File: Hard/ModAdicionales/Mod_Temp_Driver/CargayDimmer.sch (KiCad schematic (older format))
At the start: 18 parts

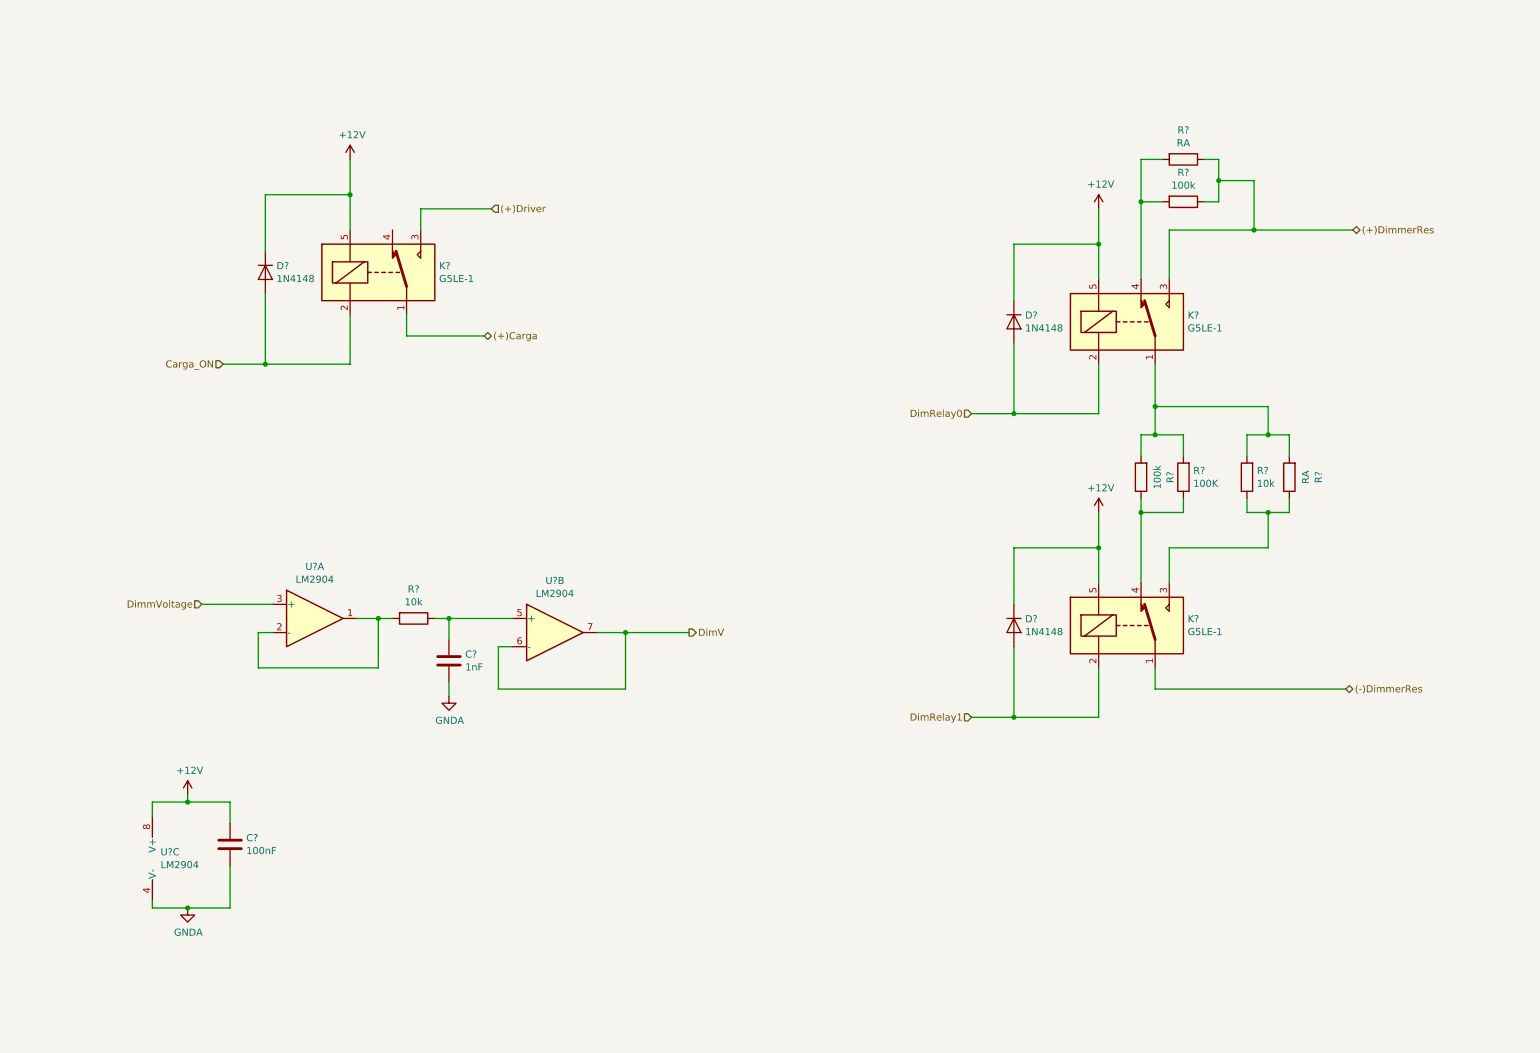
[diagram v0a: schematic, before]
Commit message: Primera correccion en modulos Adicionales y cambio de etapa de salida en modulo principal
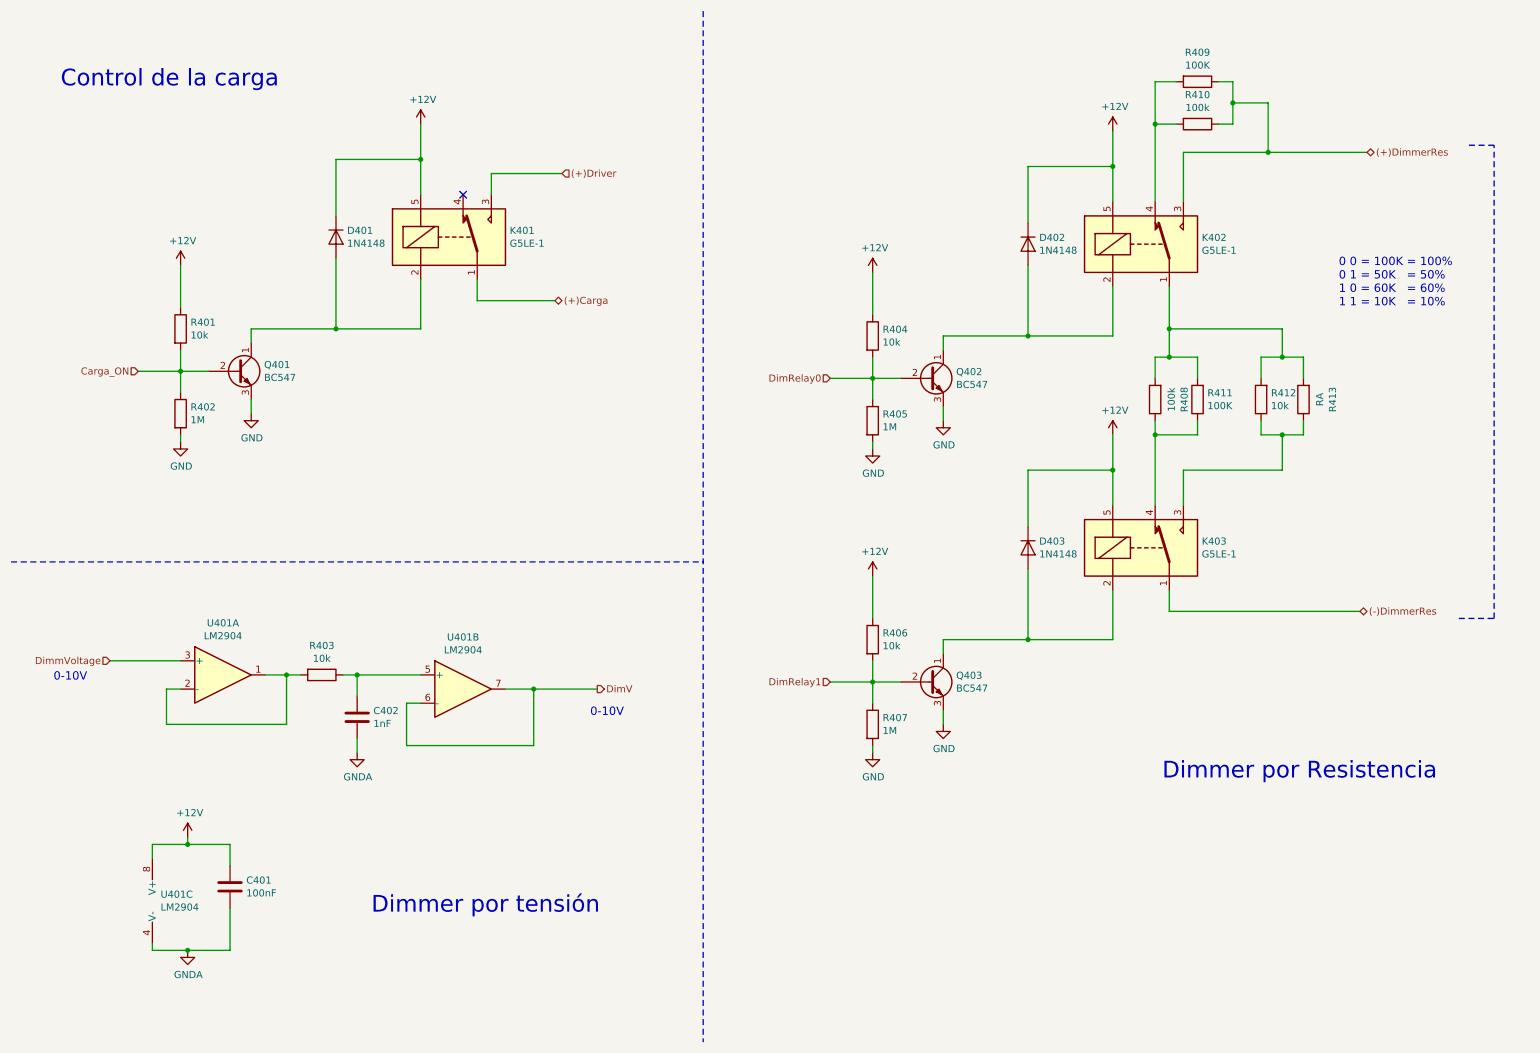
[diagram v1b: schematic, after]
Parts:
- added Q401, Q402, Q403: BC547, Package_TO_SOT_THT:TO-92_Inline, symbol Transistor_BJT:BC547
- added R401, R404, R406: 10k, Resistor_SMD:R_0805_2012Metric_Pad1.15x1.40mm_HandSolder, symbol Device:R
- added R402, R405, R407: 1M, Resistor_SMD:R_0805_2012Metric_Pad1.15x1.40mm_HandSolder, symbol Device:R
- R409: renamed from R?; value RA -> 100K
- gave numbers to parts that had none: 15
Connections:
- net +12V: now also R401.1, R404.1, R406.1
- net Carga_ON: now also Q401.2 (B), R401.2, R402.1; no longer D401.2 (A), K401.2
- net DimRelay0: now also Q402.2 (B), R404.2, R405.1; no longer D402.2 (A), K402.2
- net DimRelay1: now also Q403.2 (B), R406.2, R407.1; no longer D403.2 (A), K403.2
- new net: D402.2 (A), K402.2, Q402.1 (C)
- new net: D403.2 (A), K403.2, Q403.1 (C)
- new net: D401.2 (A), K401.2, Q401.1 (C)
- new net GND: Q401.3 (E), Q402.3 (E), Q403.3 (E), R402.2, R405.2, R407.2
- no-connect marks 0 -> 1
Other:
- note added: "0 0 = 100K = 100%\n0 1 = 50K = 50% \n1 0 = 60K = 60%\n1 1 = 10K = 10%\n"
- note added: "0-10V\n"
- note added: "Control de la carga"
- note added: "Dimmer por Resistencia\n"
- note added: "Dimmer por tensión\n"
- moved on the sheet: C401, C402, D401, D402, D403, K401, K402, K403, R403, R408, R409, R410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

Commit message: Asignacion de footprints Modulos adicionales
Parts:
- removed Q401, Q402, Q403: BC547, Package_TO_SOT_THT:TO-92_Inline, symbol Transistor_BJT:BC547
- added Q401, Q402, Q403: BC857, Package_TO_SOT_SMD:SOT-23, symbol Transistor_BJT:BC857
- R405: value 1M -> 10k
- R406: value 10k -> 1M
- U401: footprint (none) -> Package_SO:SO-8_3.9x4.9mm_P1.27mm
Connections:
- net +12V: now also R402.1, R407.1, Q401.2 (E), Q402.2 (E), Q403.2 (E); no longer D401.1 (K), D402.1 (K), D403.1 (K), K401.5, K402.5, K403.5, R401.1, R404.1
- net Carga_ON: now also R401.1; no longer R401.2, R402.1
- net DimRelay0: now also R404.1; no longer R404.2, R405.1
- net DimRelay1: now also R405.1; no longer R406.2, R407.1
- net GND: now also D401.2 (A), D402.2 (A), D403.2 (A), K401.2, K402.2, K403.2; no longer R402.2, R405.2, R407.2
- new net: Q401.1 (B), R401.2, R402.2
- new net: D401.1 (K), K401.5, Q401.3 (C)
- new net: Q402.1 (B), R404.2, R406.2
- new net: D402.1 (K), K402.5, Q402.3 (C)
- new net: Q403.1 (B), R405.2, R407.2
- new net: D403.1 (K), K403.5, Q403.3 (C)
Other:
- moved on the sheet: D401, K401, R401, R402

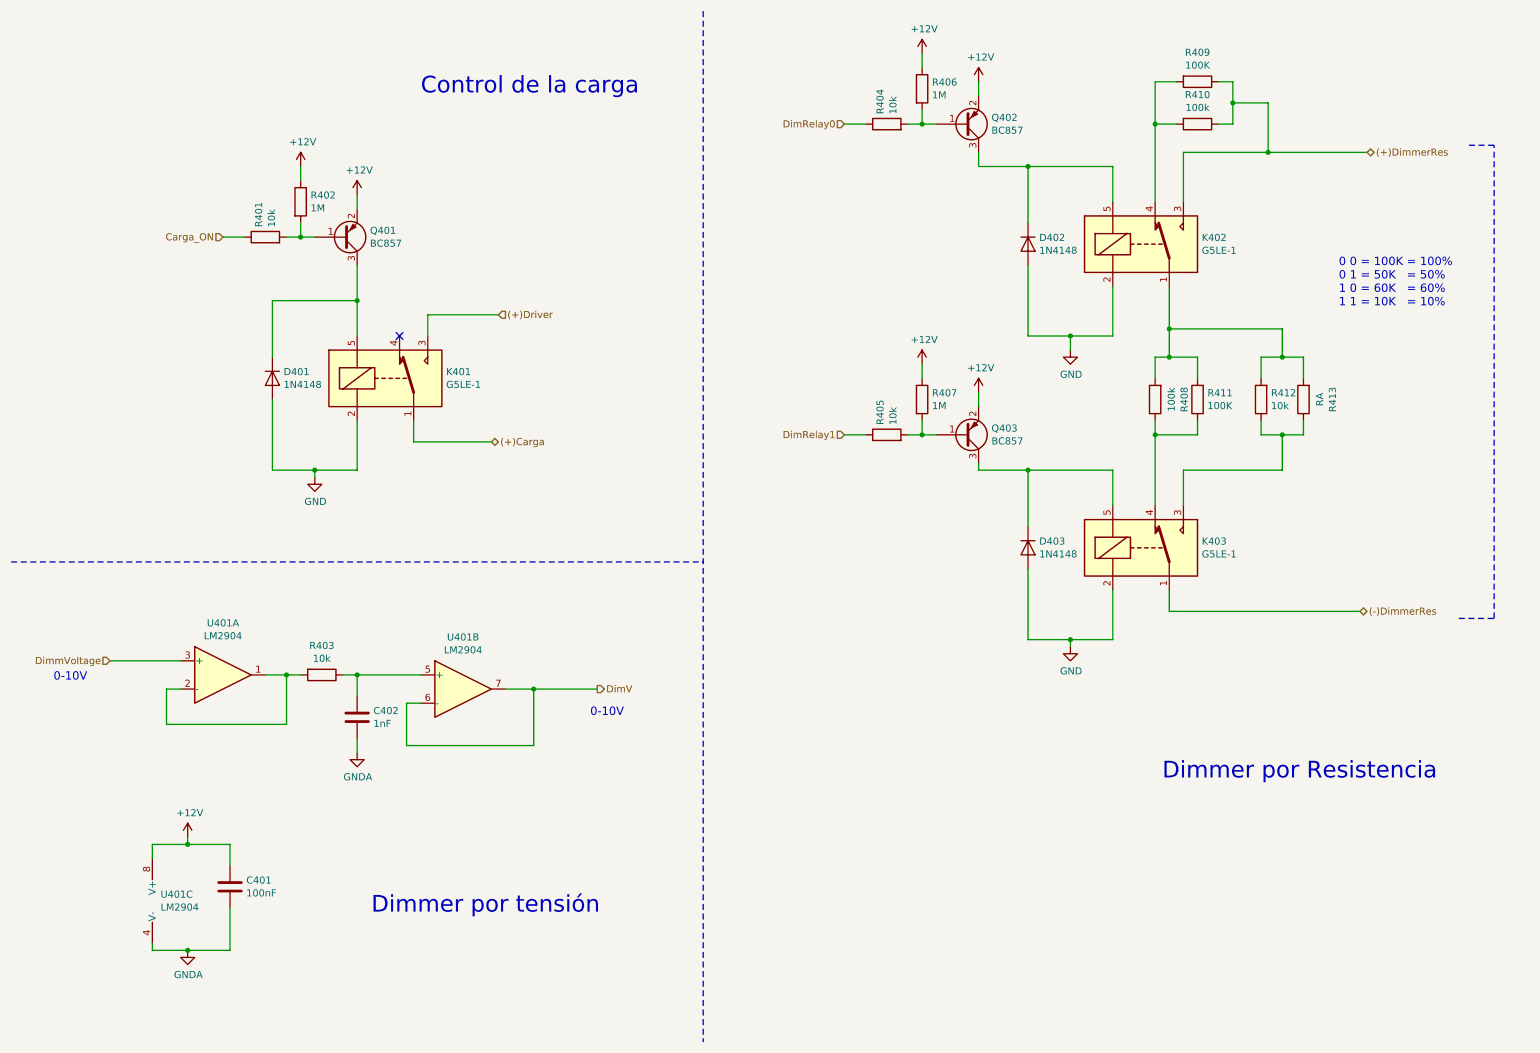
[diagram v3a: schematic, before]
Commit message: Avance en trazado de pistas Modulos Adicionales
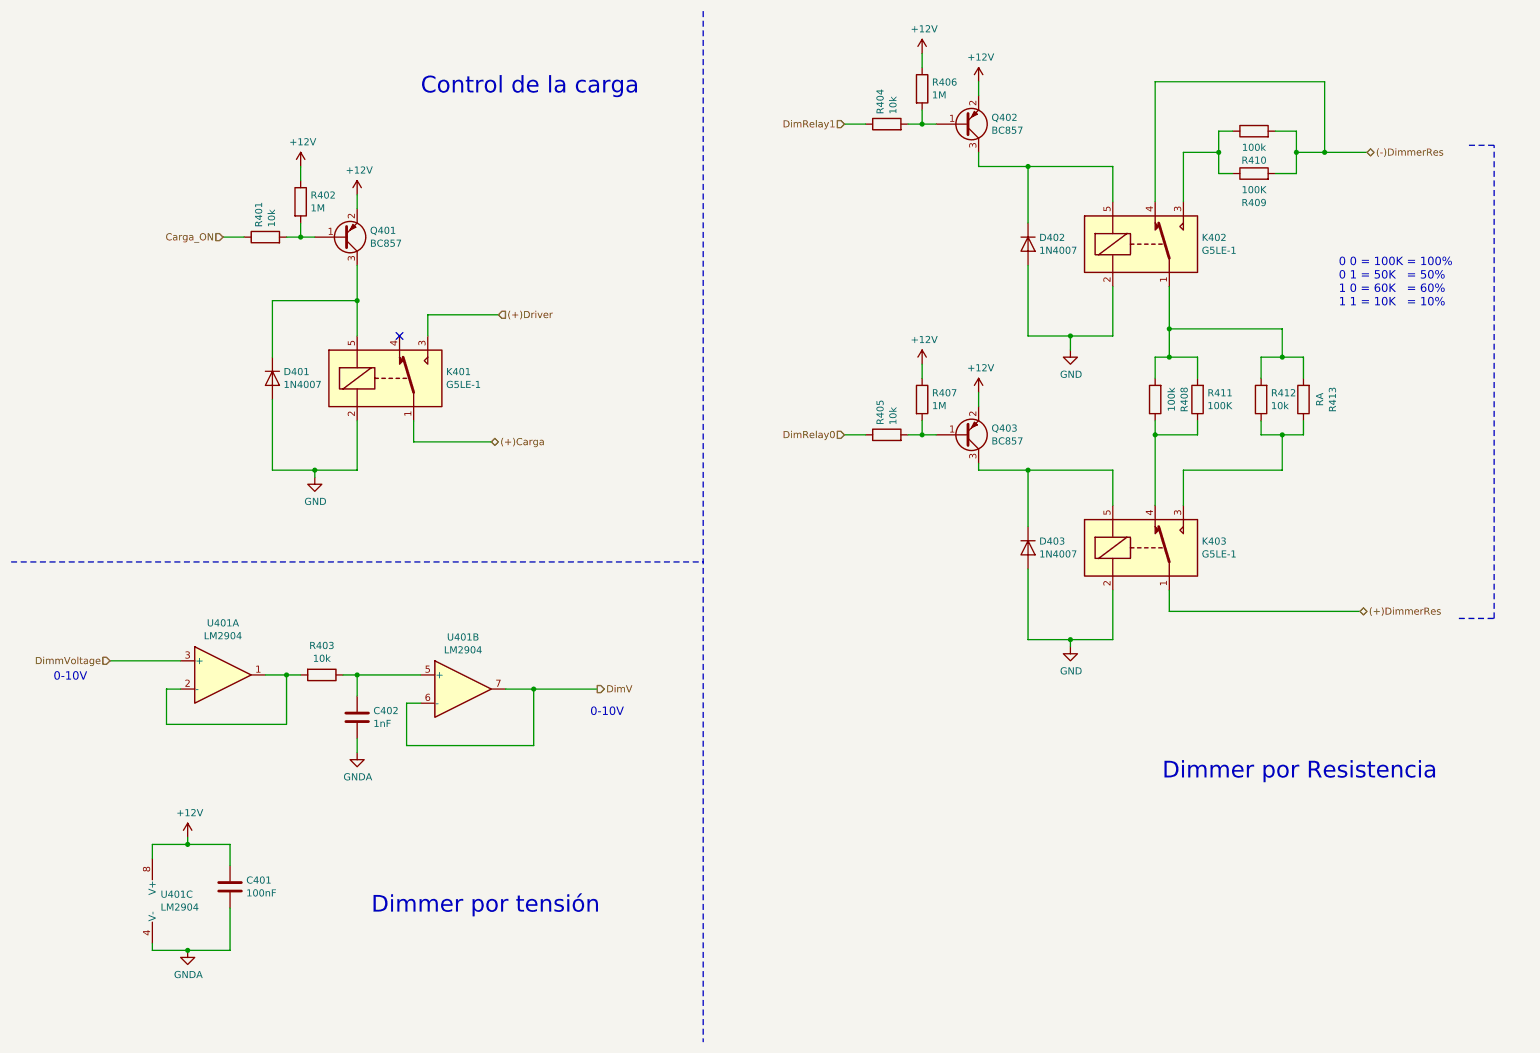
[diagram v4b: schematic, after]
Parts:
- removed D401, D402, D403: 1N4148, Diode_THT:D_DO-35_SOD27_P7.62mm_Horizontal, symbol Diode:1N4148
- added D401, D402, D403: 1N4007, Diode_THT:D_DO-41_SOD81_P10.16mm_Horizontal, symbol Diode:1N4007
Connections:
- net (+)DimmerRes: now also K403.1; no longer K402.3, R409.1, R410.1
- net (-)DimmerRes: now also K402.4, R409.2, R410.2; no longer K403.1
- net DimRelay0: now also R405.1; no longer R404.1
- net DimRelay1: now also R404.1; no longer R405.1
- net GND: now also D401.2 (A), D402.2 (A), D403.2 (A)
- net at K401.5, Q401.3 (C): now also D401.1 (K)
- net at K402.5, Q402.3 (C): now also D402.1 (K)
- net at K403.5, Q403.3 (C): now also D403.1 (K)
- new net: K402.3, R409.1, R410.1
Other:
- moved on the sheet: R409, R410
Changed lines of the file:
@@
-$EndComp
-$Comp
-L Diode:1N4148 D401
-U 1 1 5F2515E6
-P 2350 3050
-F 0 "D401" V 2304 3129 50  0000 L CNN
-F 1 "1N4148" V 2395 3129 50  0000 L CNN
-F 2 "Diode_THT:D_DO-35_SOD27_P7.62mm_Horizontal" H 2350 2875 50  0001 C CNN
-F 3 "https://assets.nexperia.com/documents/data-sheet/1N4148_1N4448.pdf" H 2350 3050 50  0001 C CNN
-	1    2350 3050
-	0    1    1    0
 $EndComp
 $Comp
@@
 	1    0    0    -1
 $EndComp
-$Comp
-L Diode:1N4148 D402
-U 1 1 5F25BECC
-P 7700 2100
-F 0 "D402" V 7654 2179 50  0000 L CNN
-F 1 "1N4148" V 7745 2179 50  0000 L CNN
-F 2 "Diode_THT:D_DO-35_SOD27_P7.62mm_Horizontal" H 7700 1925 50  0001 C CNN
-F 3 "https://assets.nexperia.com/documents/data-sheet/1N4148_1N4448.pdf" H 7700 2100 50  0001 C CNN
-	1    7700 2100
-	0    1    1    0
-$EndComp
 Wire Wire Line
 	7700 1950 7700 1550
@@
 Wire Wire Line
 	7700 2750 7700 2250
-Text HLabel 10100 1450 2    50   BiDi ~ 0
+Text HLabel 10050 4700 2    50   BiDi ~ 0
 (+)DimmerRes
-Text HLabel 6400 1250 0    50   Input ~ 0
+Text HLabel 6400 3450 0    50   Input ~ 0
 DimRelay0
 $Comp
@@
 	1    0    0    -1
 $EndComp
-$Comp
-L Diode:1N4148 D403
-U 1 1 5F25E36F
-P 7700 4250
-F 0 "D403" V 7654 4329 50  0000 L CNN
-F 1 "1N4148" V 7745 4329 50  0000 L CNN
-F 2 "Diode_THT:D_DO-35_SOD27_P7.62mm_Horizontal" H 7700 4075 50  0001 C CNN
-F 3 "https://assets.nexperia.com/documents/data-sheet/1N4148_1N4448.pdf" H 7700 4250 50  0001 C CNN
-	1    7700 4250
-	0    1    1    0
-$EndComp
 Wire Wire Line
 	7700 4100 7700 3700
@@
 Wire Wire Line
 	7700 4900 7700 4400
-Text HLabel 10050 4700 2    50   BiDi ~ 0
+Text HLabel 10100 1450 2    50   BiDi ~ 0
 (-)DimmerRes
 Wire Wire Line
 	8700 4700 8700 4550
-Text HLabel 6400 3450 0    50   Input ~ 0
+Text HLabel 6400 1250 0    50   Input ~ 0
 DimRelay1
 $Comp
 L Device:R R?
 U 1 1 5F281365
-P 8900 1250
+P 9300 1300
 AR Path="/5ED5374F/5F281365" Ref="R?"  Part="1"
 AR Path="/5ED5374F/5F0ECABF/5F281365" Ref="R?"  Part="1"
 AR Path="/5ED5374F/5F20E931/5F281365" Ref="R410"  Part="1"
-F 0 "R410" V 8693 1250 50  0000 C CNN
-F 1 "100k" V 8784 1250 50  0000 C CNN
-F 2 "Resistor_SMD:R_0805_2012Metric_Pad1.15x1.40mm_HandSolder" V 8830 1250 50  0001 C CNN
-F 3 "~" H 8900 1250 50  0001 C CNN
-	1    8900 1250
-	0    1    1    0
+F 0 "R410" V 9093 1300 50  0000 C CNN
+F 1 "100k" V 9184 1300 50  0000 C CNN
+F 2 "Resistor_SMD:R_0805_2012Metric_Pad1.15x1.40mm_HandSolder" V 9230 1300 50  0001 C CNN
+F 3 "~" H 9300 1300 50  0001 C CNN
+	1    9300 1300
+	0    -1   -1   0
 $EndComp
 $Comp
 L Device:R R?
 U 1 1 5F2819C2
-P 8900 950
+P 9300 1600
 AR Path="/5ED5374F/5F2819C2" Ref="R?"  Part="1"
 AR Path="/5ED5374F/5F0ECABF/5F2819C2" Ref="R?"  Part="1"
 AR Path="/5ED5374F/5F20E931/5F2819C2" Ref="R409"  Part="1"
-F 0 "R409" V 8693 950 50  0000 C CNN
-F 1 "100K" V 8784 950 50  0000 C CNN
-F 2 "Resistor_SMD:R_0805_2012Metric_Pad1.15x1.40mm_HandSolder" V 8830 950 50  0001 C CNN
-F 3 "~" H 8900 950 50  0001 C CNN
-	1    8900 950
-	0    1    1    0
-$EndComp
-Wire Wire Line
-	9050 950  9150 950
-Wire Wire Line
-	9150 950  9150 1100
-Wire Wire Line
-	9150 1250 9050 1250
-Wire Wire Line
-	8750 950  8600 950
-Wire Wire Line
-	8600 950  8600 1250
-Wire Wire Line
-	8600 1250 8750 1250
-Wire Wire Line
-	8600 1800 8600 1250
-Connection ~ 8600 1250
-Wire Wire Line
-	8800 1450 9400 1450
+F 0 "R409" V 9093 1600 50  0000 C CNN
+F 1 "100K" V 9184 1600 50  0000 C CNN
+F 2 "Resistor_SMD:R_0805_2012Metric_Pad1.15x1.40mm_HandSolder" V 9230 1600 50  0001 C CNN
+F 3 "~" H 9300 1600 50  0001 C CNN
+	1    9300 1600
+	0    -1   -1   0
+$EndComp
+Wire Wire Line
+	9150 1600 9050 1600
+Wire Wire Line
+	9050 1600 9050 1450
+Wire Wire Line
+	9050 1300 9150 1300
+Wire Wire Line
+	9450 1600 9600 1600
+Wire Wire Line
+	9600 1300 9450 1300
 Wire Wire Line
 	8800 1450 8800 1800
-Wire Wire Line
-	9150 1100 9400 1100
-Wire Wire Line
-	9400 1100 9400 1450
-Connection ~ 9150 1100
-Wire Wire Line
-	9150 1100 9150 1250
-Connection ~ 9400 1450
-Wire Wire Line
-	9400 1450 10100 1450
+Connection ~ 9050 1450
+Wire Wire Line
+	9050 1450 9050 1300
 $Comp
 L Device:R R?
@@
 	7350 1550 7350 1450
 Connection ~ 7700 1550
+Wire Wire Line
+	8600 950  8600 1800
+Wire Wire Line
+	9600 1600 9600 1450
+Wire Wire Line
+	9800 1450 9600 1450
+Connection ~ 9600 1450
+Wire Wire Line
+	9600 1450 9600 1300
+Wire Wire Line
+	9050 1450 8800 1450
+Wire Wire Line
+	8600 950  9800 950
+Wire Wire Line
+	9800 950  9800 1450
+Connection ~ 9800 1450
+Wire Wire Line
+	9800 1450 10100 1450
+$Comp
+L Diode:1N4007 D401
+U 1 1 5EEA7718
+P 2350 3050
+F 0 "D401" V 2304 3129 50  0000 L CNN
+F 1 "1N4007" V 2395 3129 50  0000 L CNN
+F 2 "Diode_THT:D_DO-41_SOD81_P10.16mm_Horizontal" H 2350 2875 50  0001 C CNN
+F 3 "http://www.vishay.com/docs/88503/1n4001.pdf" H 2350 3050 50  0001 C CNN
+	1    2350 3050
+	0    1    1    0
+$EndComp
+$Comp
+L Diode:1N4007 D402
+U 1 1 5EEBB598
+P 7700 2100
+F 0 "D402" V 7654 2179 50  0000 L CNN
+F 1 "1N4007" V 7745 2179 50  0000 L CNN
+F 2 "Diode_THT:D_DO-41_SOD81_P10.16mm_Horizontal" H 7700 1925 50  0001 C CNN
+F 3 "http://www.vishay.com/docs/88503/1n4001.pdf" H 7700 2100 50  0001 C CNN
+	1    7700 2100
+	0    1    1    0
+$EndComp
+$Comp
+L Diode:1N4007 D403
+U 1 1 5EEC0377
+P 7700 4250
+F 0 "D403" V 7654 4329 50  0000 L CNN
+F 1 "1N4007" V 7745 4329 50  0000 L CNN
+F 2 "Diode_THT:D_DO-41_SOD81_P10.16mm_Horizontal" H 7700 4075 50  0001 C CNN
+F 3 "http://www.vishay.com/docs/88503/1n4001.pdf" H 7700 4250 50  0001 C CNN
+	1    7700 4250
+	0    1    1    0
+$EndComp
 $EndSCHEMATC
